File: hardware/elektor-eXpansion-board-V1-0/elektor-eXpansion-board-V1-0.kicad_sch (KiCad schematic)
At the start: 29 parts, among them J1 IO1, J10 5V-GND, J11 Qwiic, J12 Qwiic, J13 5442219, J2 IO3, J3 IO4, J4 IO2, J5 I2C.., J6 I2C.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

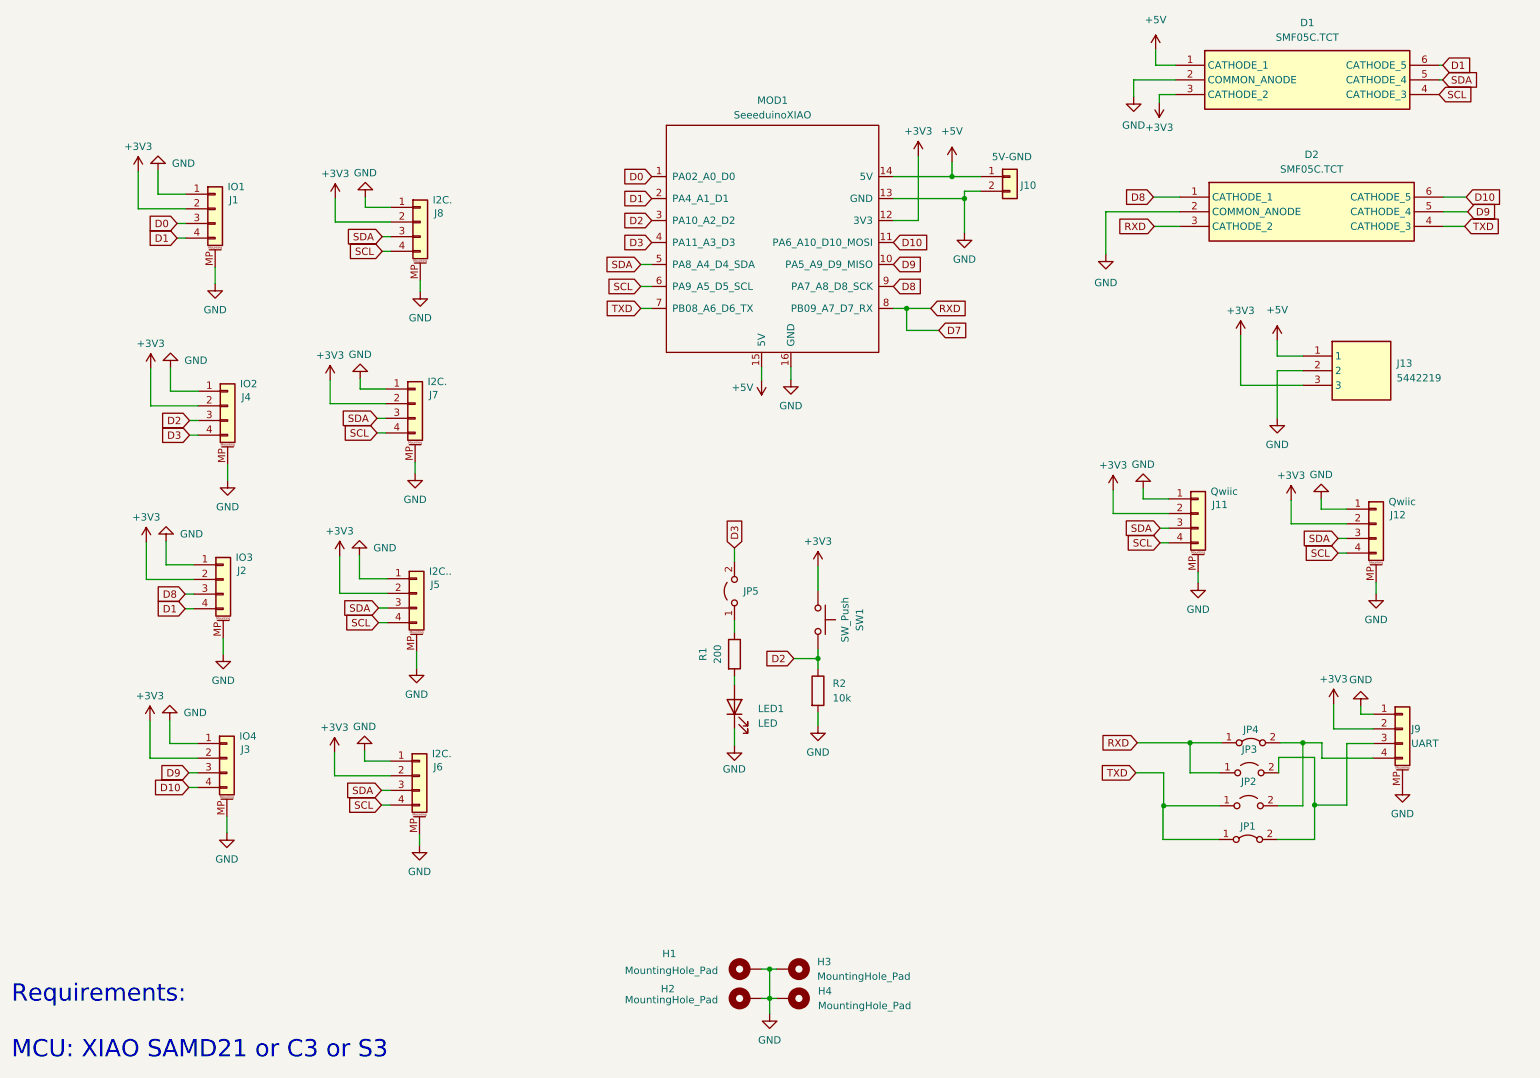
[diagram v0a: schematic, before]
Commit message: v1.01
feat: Release v1.01 of Elektor eXpansion Board

- Improved overall PCB layout for better performance and usability.
- Enhanced Xiao board footprint to support both SMD and THT soldering.
- Optimized power, I2C, and UART track routing for improved signal integrity.
- Adjusted placement of button and LED for better accessibility.
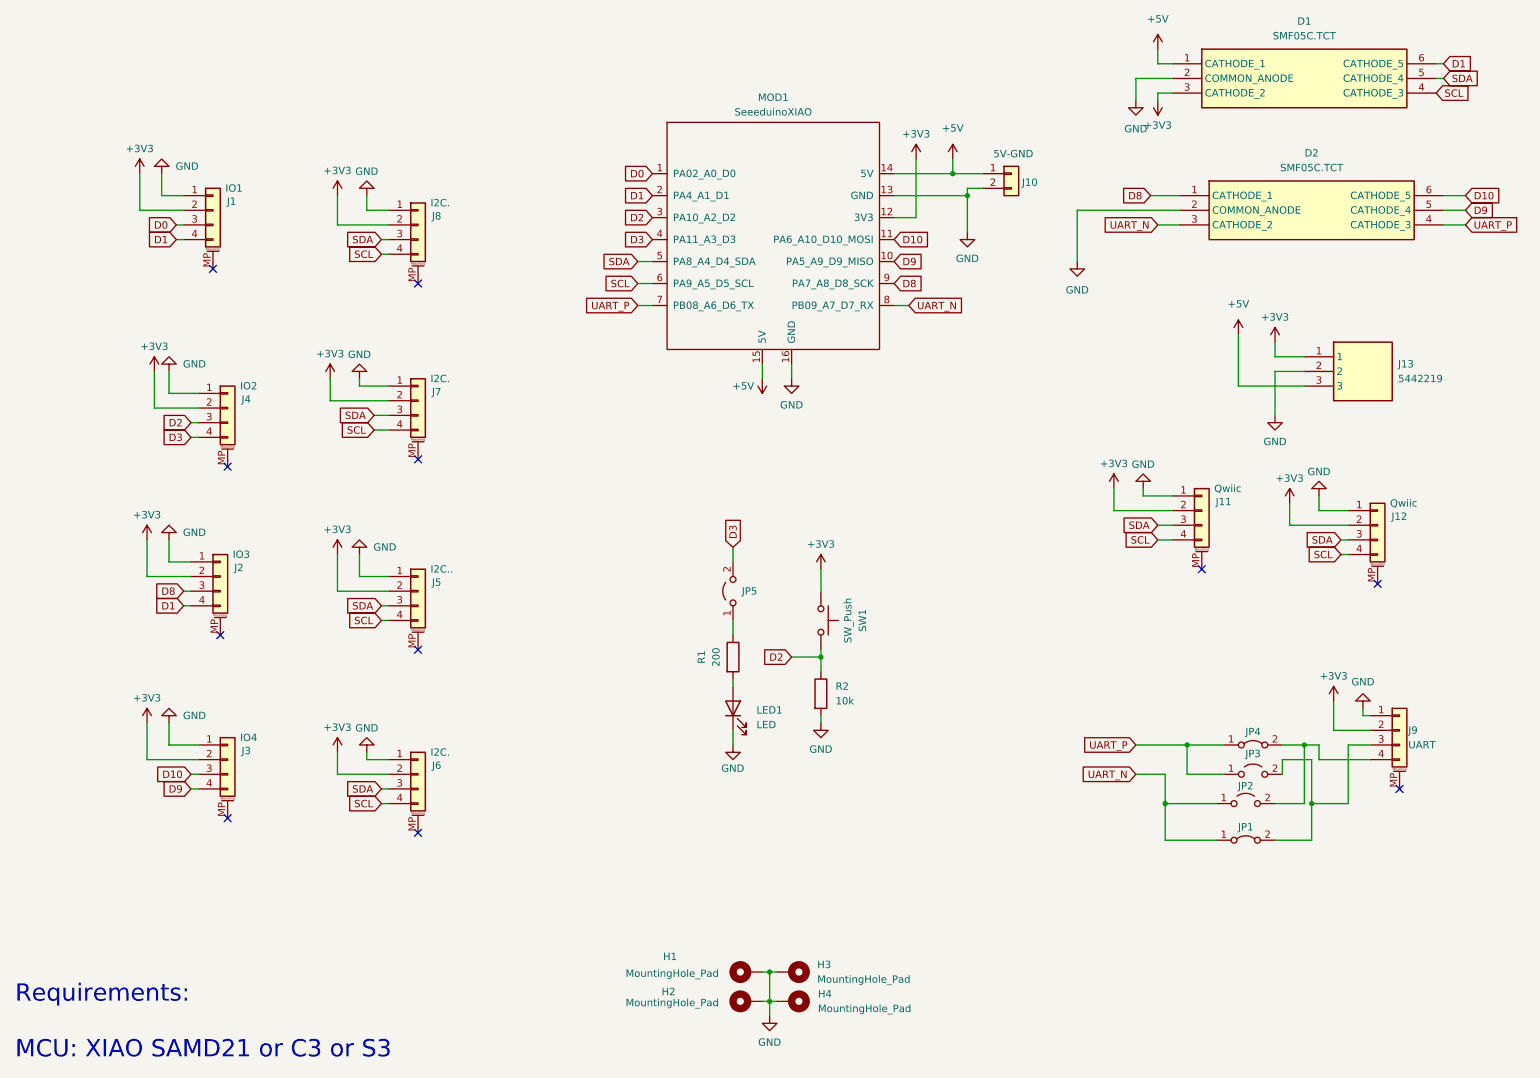
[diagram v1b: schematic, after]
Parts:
- MOD1: footprint footprints:Seeeduino XIAO-MOUDLE14P-2.54-21X17.8MM -> lib:XIAO-ESP32C3-DIP
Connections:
- net +3V3: now also J13.1; no longer J13.3
- net +5V: now also J13.3; no longer J13.1
- net D10: now also J3.3 (Pin_3); no longer J3.4 (Pin_4)
- net D9: now also J3.4 (Pin_4); no longer J3.3 (Pin_3)
- net GND: no longer J1.MP (MountPin), J11.MP (MountPin), J12.MP (MountPin), J2.MP (MountPin), J3.MP (MountPin), J4.MP (MountPin), J5.MP (MountPin), J6.MP (MountPin), J7.MP (MountPin), J8.MP (MountPin), J9.MP (MountPin)
- net D7 renamed UART_N
- net UART_N: now also JP1.1 (A), JP2.1 (A); no longer JP3.1 (A), JP4.1 (A)
- net TXD renamed UART_P
- net UART_P: now also JP3.1 (A), JP4.1 (A); no longer JP1.1 (A), JP2.1 (A)
- no-connect marks 0 -> 11
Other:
- moved on the sheet: D1, H1, H2, H3, H4, J10, J11, J2, J7, J8, J9, JP2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
